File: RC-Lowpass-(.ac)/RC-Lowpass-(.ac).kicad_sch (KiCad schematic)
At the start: 3 parts

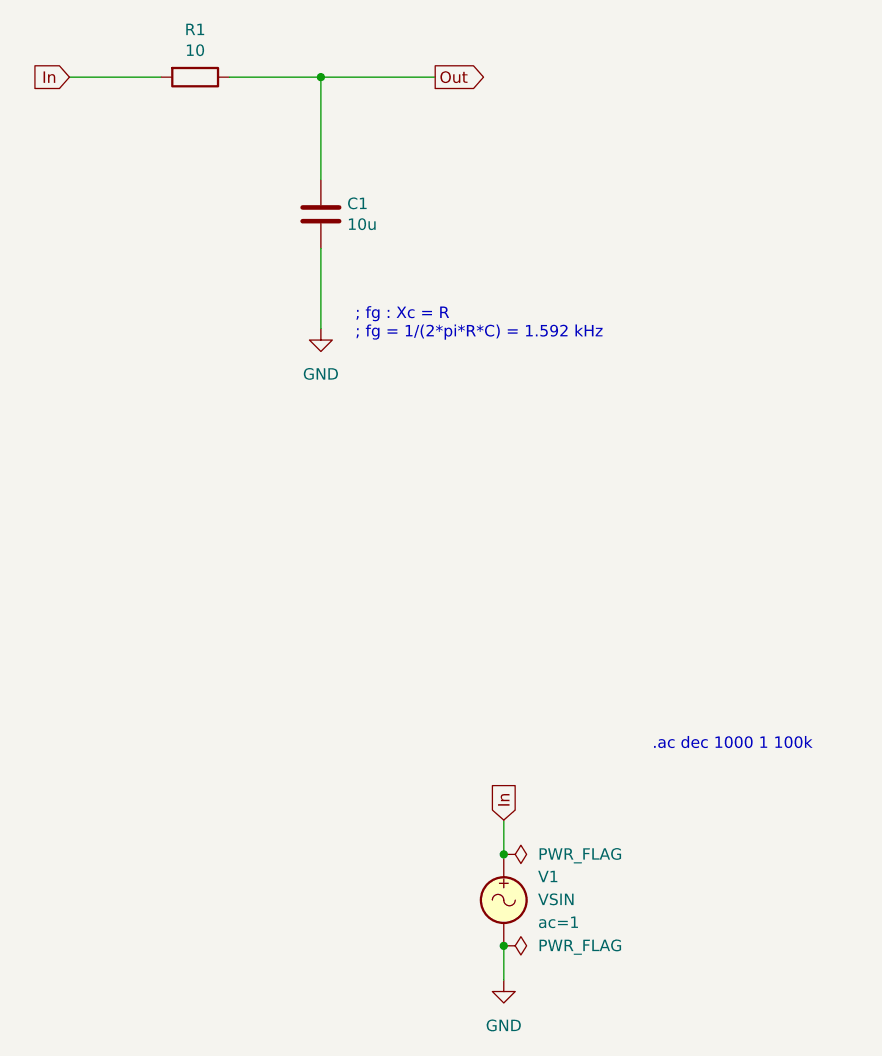
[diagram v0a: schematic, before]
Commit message: Updated all schematics and prepared for KiCad 8.0
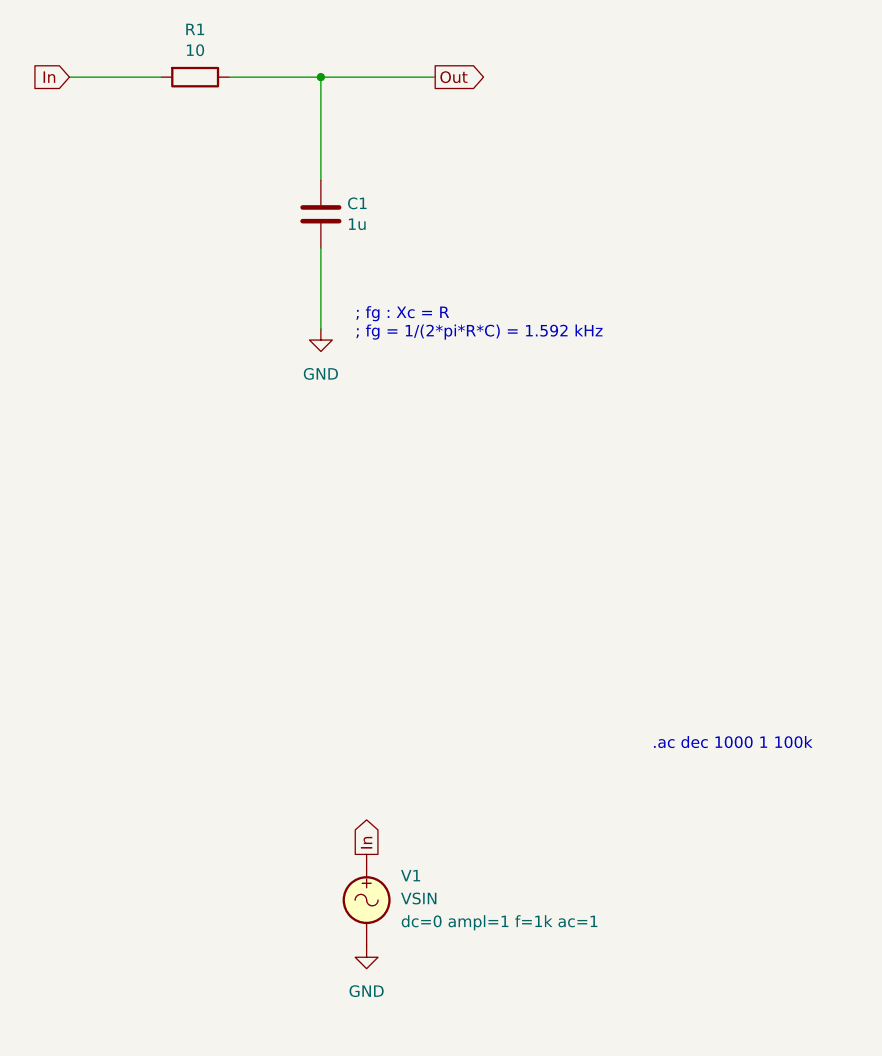
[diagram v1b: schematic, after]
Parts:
- C1: value 10u -> 1u
